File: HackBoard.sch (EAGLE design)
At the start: 45 parts, among them J1 USB MICRO, J2 8x1F-H8.5, J3 8x1F-H8.5, J4 6x1F-H8.5, P13 Yellow, U1 ATMEGA32U4-XUMU, U2 ATMEGA32U4-XUAU, U3 LP2985-33DBVR, Y1 16MHz KX-7

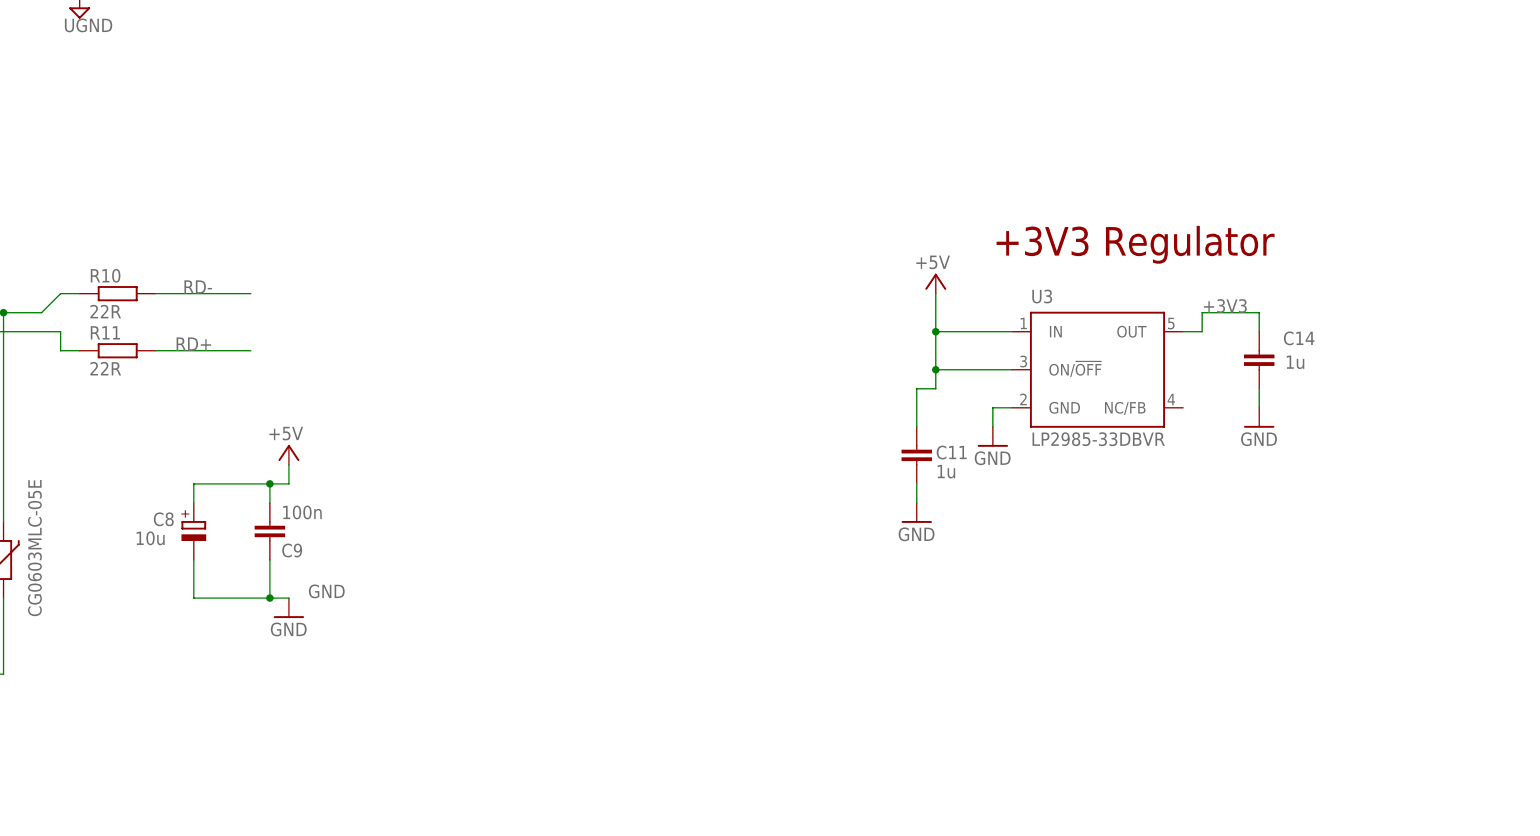
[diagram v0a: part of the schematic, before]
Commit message: Adición de 2 switch y 3 leds
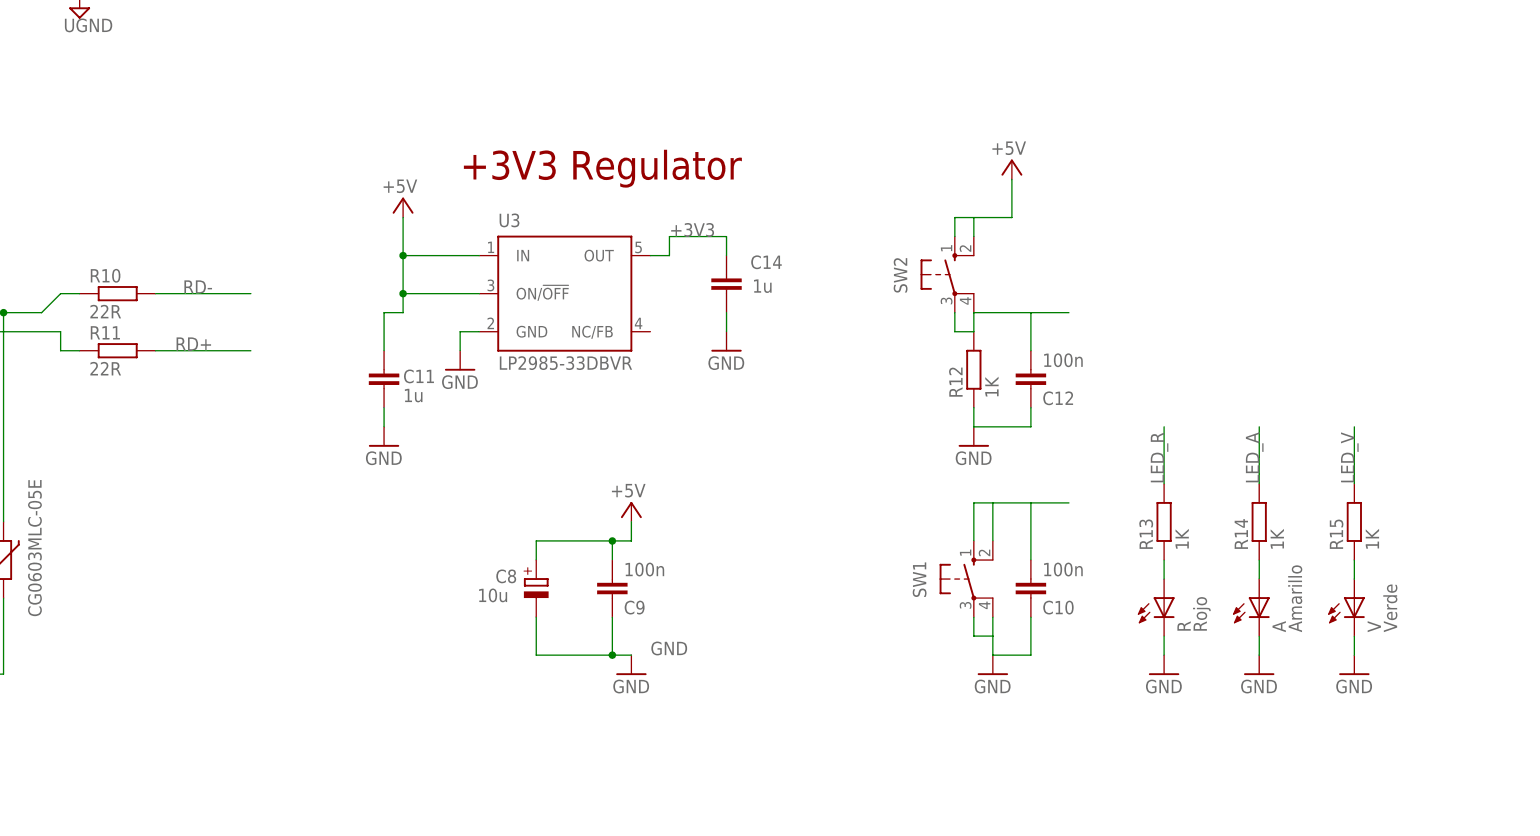
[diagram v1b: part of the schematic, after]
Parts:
- added A: Amarillo, led:LEDCHIPLED_0805
- added C10, C12: 100n, rcl:C-EUC0805
- added R: Rojo, led:LEDCHIPLED_0805
- added R12, R13, R14, R15: 1K, resistor:R-EU_M0805
- added SW1, SW2: (no value), switch-omron:10-XX
- added V: Verde, led:LEDCHIPLED_0805
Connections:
- new net LED_A: R14.2
- new net LED_R: R13.2
- new net LED_V: R15.2
- new net N$10: R15.1, V.A
- new net N$8: R.A, R13.1
- new net N$9: A.A, R14.1
- new net SW1: C10.2, SW1.S, SW1.S1
- new net SW2: C12.2, R12.2, SW2.P, SW2.P1
- net +5V: now also SW2.S, SW2.S1
- net GND: now also A.C, C10.1, C12.1, R.C, R12.1, SW1.P, SW1.P1, V.C
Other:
- moved on the sheet: C11, C14, C8, C9, U3

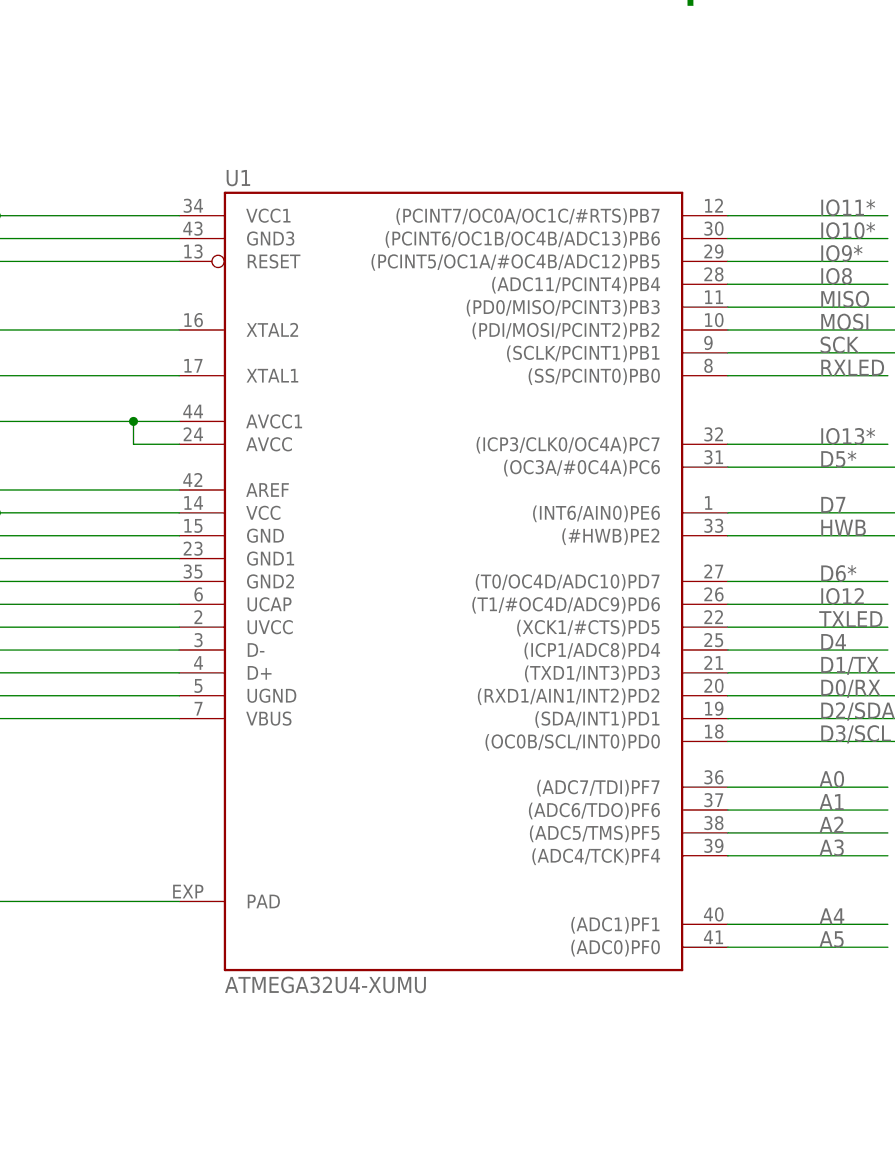
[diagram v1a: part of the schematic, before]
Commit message: Se elimina Micro con encapsulado QFN
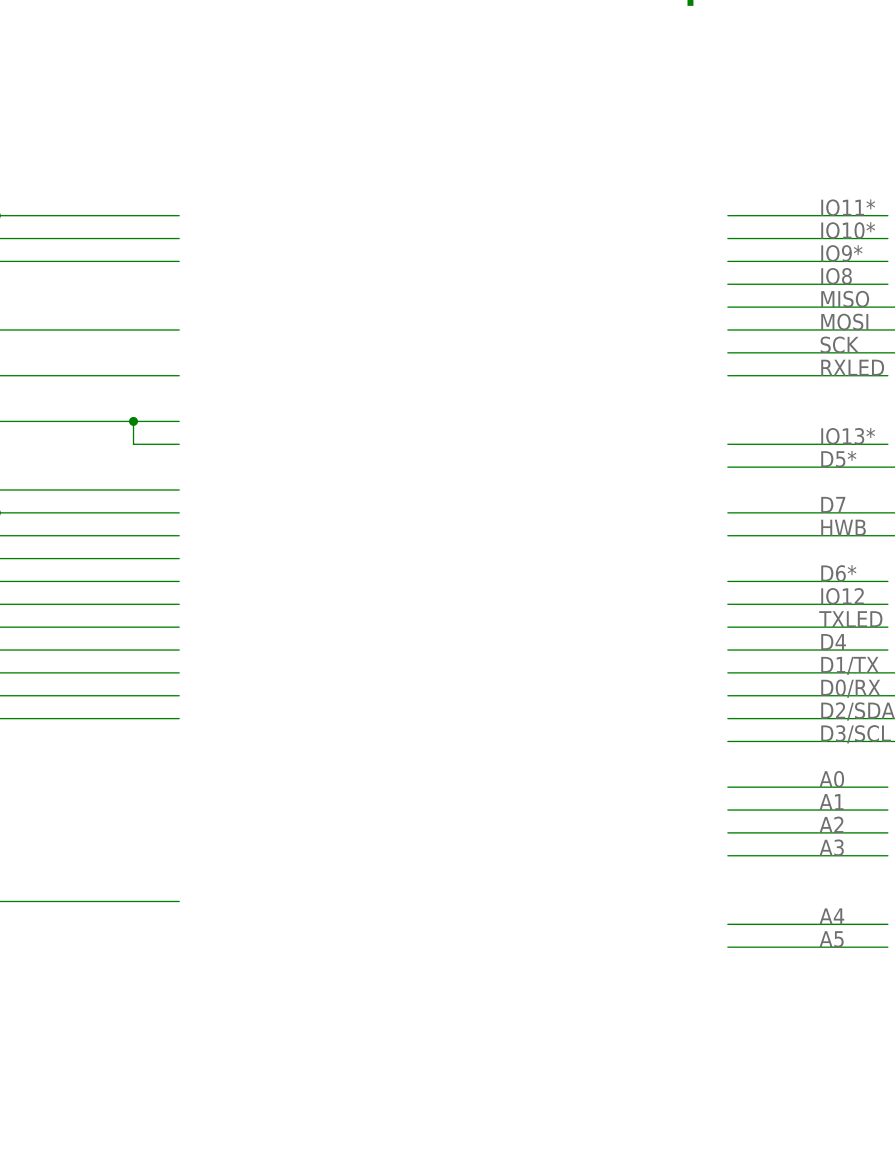
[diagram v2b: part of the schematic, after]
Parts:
- removed U1: ATMEGA32U4-XUMU, SmartPrj:ATMEGA32U4-XUMU
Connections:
- net +5V: no longer U1.UVCC, U1.VBUS, U1.VCC, U1.VCC1
- net A0: no longer U1.(ADC7/TDI)PF7
- net A1: no longer U1.(ADC6/TDO)PF6
- net A2: no longer U1.(ADC5/TMS)PF5
- net A3: no longer U1.(ADC4/TCK)PF4
- net A4: no longer U1.(ADC1)PF1
- net A5: no longer U1.(ADC0)PF0
- net AGND: no longer U1.GND3
- net AREF: no longer U1.AREF
- net AVCC: no longer U1.AVCC, U1.AVCC1
- net D0/RX: no longer U1.(RXD1/AIN1/INT2)PD2
- net D1/TX: no longer U1.(TXD1/INT3)PD3
- net D2/SDA: no longer U1.(SDA/INT1)PD1
- net D3/SCL: no longer U1.(OC0B/SCL/INT0)PD0
- net D4: no longer U1.(ICP1/ADC8)PD4
- net D5*: no longer U1.(OC3A/#0C4A)PC6
- net D6*: no longer U1.(T0/OC4D/ADC10)PD7
- net D7: no longer U1.(INT6/AIN0)PE6
- net GND: no longer U1.GND, U1.GND1, U1.GND2, U1.PAD
- net HWB: no longer U1.(#HWB)PE2
- net IO10*: no longer U1.(PCINT6/OC1B/OC4B/ADC13)PB6
- net IO11*: no longer U1.(PCINT7/OC0A/OC1C/#RTS)PB7
- net IO12: no longer U1.(T1/#OC4D/ADC9)PD6
- net IO13*: no longer U1.(ICP3/CLK0/OC4A)PC7
- net IO8: no longer U1.(ADC11/PCINT4)PB4
- net IO9*: no longer U1.(PCINT5/OC1A/#OC4B/ADC12)PB5
- net MISO: no longer U1.(PD0/MISO/PCINT3)PB3
- net MOSI: no longer U1.(PDI/MOSI/PCINT2)PB2
- net RD+: no longer U1.D+
- net RD-: no longer U1.D-
- net RESET: no longer U1.RESET
- net RXLED: no longer U1.(SS/PCINT0)PB0
- net SCK: no longer U1.(SCLK/PCINT1)PB1
- net TXLED: no longer U1.(XCK1/#CTS)PD5
- net UCAP: no longer U1.UCAP
- net UGND: no longer U1.UGND
- net XTAL1: no longer U1.XTAL1
- net XTAL2: no longer U1.XTAL2
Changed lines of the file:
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@@
 <part name="C1" library="rcl" deviceset="C-EU" device="C0805" value="100n"/>
 <part name="GND3" library="supply1" deviceset="GND" device=""/>
-<part name="U1" library="SmartPrj" deviceset="ATMEGA32U4-XU" device="MU"/>
 <part name="U2" library="SmartPrj" deviceset="ATMEGA32U4-XU" device="AU"/>
 <part name="C8" library="rcl" deviceset="CPOL-EU" device="SMCB" value="10u"/>
@@
 <instance part="C1" gate="G$1" x="-50.8" y="137.16"/>
 <instance part="GND3" gate="1" x="129.54" y="48.26"/>
-<instance part="U1" gate="G$1" x="17.78" y="104.14"/>
 <instance part="U2" gate="G$1" x="175.26" y="104.14"/>
 <instance part="C8" gate="G$1" x="-2.54" y="-38.1" smashed="yes">
@@
 <pinref part="L1" gate="G$1" pin="1"/>
 <pinref part="U$36" gate="G$1" pin="+5V"/>
-<pinref part="U1" gate="G$1" pin="UVCC"/>
-<pinref part="U1" gate="G$1" pin="VCC"/>
-<pinref part="U1" gate="G$1" pin="VCC1"/>
 </segment>
 <segment>
@@
 <wire x1="-38.1" y1="58.42" x2="-38.1" y2="63.5" width="0.1524" layer="91"/>
 <label x="-35.56" y="58.42" size="1.778" layer="95"/>
-<pinref part="U1" gate="G$1" pin="VBUS"/>
 <pinref part="P+6" gate="1" pin="+5V"/>
 </segment>
@@
 <wire x1="-38.1" y1="50.8" x2="-38.1" y2="45.72" width="0.1524" layer="91"/>
 <label x="-35.56" y="50.8" size="1.778" layer="95"/>
-<pinref part="U1" gate="G$1" pin="PAD"/>
 <pinref part="GND4" gate="1" pin="GND"/>
 </segment>
@@
 <label x="-30.48" y="86.36" size="1.778" layer="95" rot="R90"/>
 <pinref part="U$30" gate="G$1" pin="COM"/>
-<pinref part="U1" gate="G$1" pin="GND"/>
-<pinref part="U1" gate="G$1" pin="GND1"/>
-<pinref part="U1" gate="G$1" pin="GND2"/>
 </segment>
 <segment>
@@
 <label x="-55.88" y="96.52" size="1.778" layer="95"/>
 <pinref part="C6" gate="G$1" pin="2"/>
-<pinref part="U1" gate="G$1" pin="AREF"/>
 </segment>
 <segment>
@@
 <label x="-78.74" y="119.38" size="1.778" layer="95"/>
 <pinref part="ICSP" gate="A" pin="5"/>
-<pinref part="U1" gate="G$1" pin="RESET"/>
 <pinref part="RESET" gate="1" pin="P"/>
 <pinref part="RESET" gate="1" pin="P1"/>
@@
 <wire x1="81.28" y1="111.76" x2="53.34" y2="111.76" width="0.1524" layer="91"/>
 <label x="63.5" y="111.76" size="1.778" layer="95"/>
-<pinref part="U1" gate="G$1" pin="(SCLK/PCINT1)PB1"/>
 </segment>
 <segment>
@@
 <wire x1="81.28" y1="116.84" x2="53.34" y2="116.84" width="0.1524" layer="91"/>
 <label x="63.5" y="116.84" size="1.778" layer="95"/>
-<pinref part="U1" gate="G$1" pin="(PD0/MISO/PCINT3)PB3"/>
 </segment>
 <segment>
@@
 <wire x1="81.28" y1="114.3" x2="53.34" y2="114.3" width="0.1524" layer="91"/>
 <label x="63.5" y="114.3" size="1.778" layer="95"/>
-<pinref part="U1" gate="G$1" pin="(PDI/MOSI/PCINT2)PB2"/>
 </segment>
 <segment>
@@
 <label x="-50.8" y="114.3" size="1.778" layer="95"/>
 <pinref part="R1" gate="G$1" pin="2"/>
-<pinref part="U1" gate="G$1" pin="XTAL2"/>
 <pinref part="C3" gate="G$1" pin="2"/>
 <pinref part="Y1" gate="G$1" pin="C2"/>
@@
 <label x="-50.8" y="109.22" size="1.778" layer="95"/>
 <pinref part="R1" gate="G$1" pin="1"/>
-<pinref part="U1" gate="G$1" pin="XTAL1"/>
 <pinref part="C4" gate="G$1" pin="1"/>
 <pinref part="Y1" gate="G$1" pin="C1"/>
@@
 <wire x1="-7.62" y1="78.74" x2="-45.72" y2="78.74" width="0.1524" layer="91"/>
 <label x="-40.64" y="78.74" size="1.778" layer="95"/>
-<pinref part="U1" gate="G$1" pin="D-"/>
 </segment>
 <segment>
@@
 <wire x1="-7.62" y1="76.2" x2="-45.72" y2="76.2" width="0.1524" layer="91"/>
 <label x="-40.64" y="76.2" size="1.778" layer="95"/>
-<pinref part="U1" gate="G$1" pin="D+"/>
 </segment>
 <segment>
@@
 <pinref part="R3" gate="G$1" pin="2"/>
 <pinref part="C7" gate="G$1" pin="2"/>
-<pinref part="U1" gate="G$1" pin="UGND"/>
 </segment>
 <segment>
@@
 <wire x1="81.28" y1="71.12" x2="53.34" y2="71.12" width="0.1524" layer="91"/>
 <label x="63.5" y="71.12" size="1.778" layer="95"/>
-<pinref part="U1" gate="G$1" pin="(SDA/INT1)PD1"/>
 </segment>
 </net>
@@
 <wire x1="71.12" y1="83.82" x2="53.34" y2="83.82" width="0.1524" layer="91"/>
 <label x="63.5" y="83.82" size="1.778" layer="95"/>
-<pinref part="U1" gate="G$1" pin="(T1/#OC4D/ADC9)PD6"/>
 </segment>
 <segment>
@@
 <wire x1="81.28" y1="68.58" x2="53.34" y2="68.58" width="0.1524" layer="91"/>
 <label x="63.5" y="68.58" size="1.778" layer="95"/>
-<pinref part="U1" gate="G$1" pin="(OC0B/SCL/INT0)PD0"/>
 </segment>
 </net>
@@
 <wire x1="81.28" y1="76.2" x2="53.34" y2="76.2" width="0.1524" layer="91"/>
 <label x="63.5" y="76.2" size="1.778" layer="95"/>
-<pinref part="U1" gate="G$1" pin="(TXD1/INT3)PD3"/>
 </segment>
 <segment>
@@
 <wire x1="71.12" y1="127" x2="53.34" y2="127" width="0.1524" layer="91"/>
 <label x="63.5" y="127" size="1.778" layer="95"/>
-<pinref part="U1" gate="G$1" pin="(PCINT7/OC0A/OC1C/#RTS)PB7"/>
 </segment>
 <segment>
@@
 <wire x1="71.12" y1="121.92" x2="53.34" y2="121.92" width="0.1524" layer="91"/>
 <label x="63.5" y="121.92" size="1.778" layer="95"/>
-<pinref part="U1" gate="G$1" pin="(PCINT5/OC1A/#OC4B/ADC12)PB5"/>
 </segment>
 <segment>
@@
 <wire x1="71.12" y1="124.46" x2="53.34" y2="124.46" width="0.1524" layer="91"/>
 <label x="63.5" y="124.46" size="1.778" layer="95"/>
-<pinref part="U1" gate="G$1" pin="(PCINT6/OC1B/OC4B/ADC13)PB6"/>
 </segment>
 <segment>
@@
 <label x="236.22" y="-45.72" size="1.778" layer="95" rot="MR270"/>
 <pinref part="J4" gate="A" pin="4"/>
-<pinref part="U1" gate="G$1" pin="(ADC4/TCK)PF4"/>
 <pinref part="JP3" gate="A" pin="4"/>
 <wire x1="236.22" y1="-63.5" x2="236.22" y2="-76.2" width="0.1524" layer="91"/>
@@
 <label x="238.76" y="-45.72" size="1.778" layer="95" rot="MR270"/>
 <pinref part="J4" gate="A" pin="3"/>
-<pinref part="U1" gate="G$1" pin="(ADC5/TMS)PF5"/>
 <pinref part="JP3" gate="A" pin="3"/>
 <wire x1="238.76" y1="-63.5" x2="238.76" y2="-76.2" width="0.1524" layer="91"/>
@@
 <label x="241.3" y="-45.72" size="1.778" layer="95" rot="MR270"/>
 <pinref part="J4" gate="A" pin="2"/>
-<pinref part="U1" gate="G$1" pin="(ADC6/TDO)PF6"/>
 <pinref part="JP3" gate="A" pin="2"/>
 <wire x1="241.3" y1="-63.5" x2="241.3" y2="-76.2" width="0.1524" layer="91"/>
@@
 <wire x1="53.34" y1="63.5" x2="71.12" y2="63.5" width="0.1524" layer="91"/>
 <label x="63.5" y="63.5" size="1.778" layer="95"/>
-<pinref part="U1" gate="G$1" pin="(ADC7/TDI)PF7"/>
 </segment>
 <segment>
@@
 <label x="233.68" y="-45.72" size="1.778" layer="95" rot="MR270"/>
 <pinref part="J4" gate="A" pin="5"/>
-<pinref part="U1" gate="G$1" pin="(ADC1)PF1"/>
 <pinref part="JP3" gate="A" pin="5"/>
 <wire x1="233.68" y1="-63.5" x2="233.68" y2="-76.2" width="0.1524" layer="91"/>
@@
 <label x="231.14" y="-45.72" size="1.778" layer="95" rot="MR270"/>
 <pinref part="J4" gate="A" pin="6"/>
-<pinref part="U1" gate="G$1" pin="(ADC0)PF0"/>
 <pinref part="JP3" gate="A" pin="6"/>
 <wire x1="231.14" y1="-76.2" x2="231.14" y2="-63.5" width="0.1524" layer="91"/>
@@
 <wire x1="73.66" y1="99.06" x2="53.34" y2="99.06" width="0.1524" layer="91"/>
 <label x="63.5" y="99.06" size="1.778" layer="95"/>
-<pinref part="U1" gate="G$1" pin="(OC3A/#0C4A)PC6"/>
 </segment>
 </net>
@@
 <wire x1="81.28" y1="73.66" x2="53.34" y2="73.66" width="0.1524" layer="91"/>
 <label x="63.5" y="73.66" size="1.778" layer="95"/>
-<pinref part="U1" gate="G$1" pin="(RXD1/AIN1/INT2)PD2"/>
 </segment>
 <segment>
@@
 <wire x1="-7.62" y1="124.46" x2="-38.1" y2="124.46" width="0.1524" layer="91"/>
 <label x="-35.56" y="124.46" size="1.778" layer="95"/>
-<pinref part="U1" gate="G$1" pin="GND3"/>
 </segment>
 <segment>
@@
 <wire x1="53.34" y1="109.22" x2="71.12" y2="109.22" width="0.1524" layer="91"/>
 <label x="63.5" y="109.22" size="1.778" layer="95"/>
-<pinref part="U1" gate="G$1" pin="(SS/PCINT0)PB0"/>
 </segment>
 <segment>
@@
 <wire x1="71.12" y1="86.36" x2="53.34" y2="86.36" width="0.1524" layer="91"/>
 <label x="63.5" y="86.36" size="1.778" layer="95"/>
-<pinref part="U1" gate="G$1" pin="(T0/OC4D/ADC10)PD7"/>
 </segment>
 <segment>
@@
 <wire x1="71.12" y1="101.6" x2="53.34" y2="101.6" width="0.1524" layer="91"/>
 <label x="63.5" y="101.6" size="1.778" layer="95"/>
-<pinref part="U1" gate="G$1" pin="(ICP3/CLK0/OC4A)PC7"/>
 </segment>
 <segment>
@@
 <wire x1="53.34" y1="119.38" x2="71.12" y2="119.38" width="0.1524" layer="91"/>
 <label x="63.5" y="119.38" size="1.778" layer="95"/>
-<pinref part="U1" gate="G$1" pin="(ADC11/PCINT4)PB4"/>
 </segment>
 <segment>
@@
 <wire x1="73.66" y1="93.98" x2="53.34" y2="93.98" width="0.1524" layer="91"/>
 <label x="63.5" y="93.98" size="1.778" layer="95"/>
-<pinref part="U1" gate="G$1" pin="(INT6/AIN0)PE6"/>
 </segment>
 </net>
@@
 <pinref part="L1" gate="G$1" pin="2"/>
 <pinref part="C5" gate="G$1" pin="1"/>
-<pinref part="U1" gate="G$1" pin="AVCC1"/>
-<pinref part="U1" gate="G$1" pin="AVCC"/>
 </segment>
 <segment>
@@
 <label x="-40.64" y="83.82" size="1.778" layer="95"/>
 <pinref part="C7" gate="G$1" pin="1"/>
-<pinref part="U1" gate="G$1" pin="UCAP"/>
 </segment>
 <segment>
@@
 <wire x1="53.34" y1="91.44" x2="83.82" y2="91.44" width="0.1524" layer="91"/>
 <label x="63.5" y="91.44" size="1.778" layer="95"/>
-<pinref part="U1" gate="G$1" pin="(#HWB)PE2"/>
 </segment>
 </net>
@@
 <wire x1="53.34" y1="78.74" x2="71.12" y2="78.74" width="0.1524" layer="91"/>
 <label x="63.5" y="78.74" size="1.778" layer="95"/>
-<pinref part="U1" gate="G$1" pin="(ICP1/ADC8)PD4"/>
 </segment>
 <segment>
@@
 <wire x1="71.12" y1="81.28" x2="53.34" y2="81.28" width="0.1524" layer="91"/>
 <label x="63.5" y="81.28" size="1.778" layer="95"/>
-<pinref part="U1" gate="G$1" pin="(XCK1/#CTS)PD5"/>
-</segment>
-</net>
+</segment>
+</net>
